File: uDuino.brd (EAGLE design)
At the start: 86.4 x 26.3 mm, 20 parts, among them IC1 LM7805, IC2 ATMEGA328, J1 POWER_JACK", Q1 16MHZ

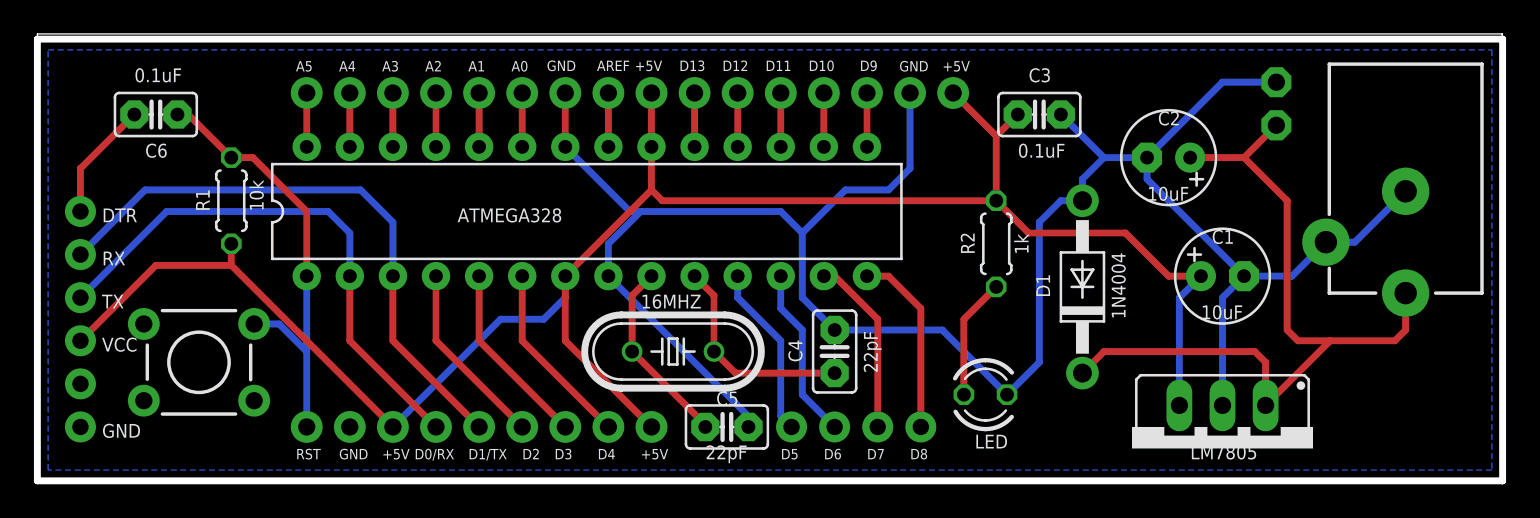
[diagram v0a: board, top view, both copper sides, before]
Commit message: Added LED at D13
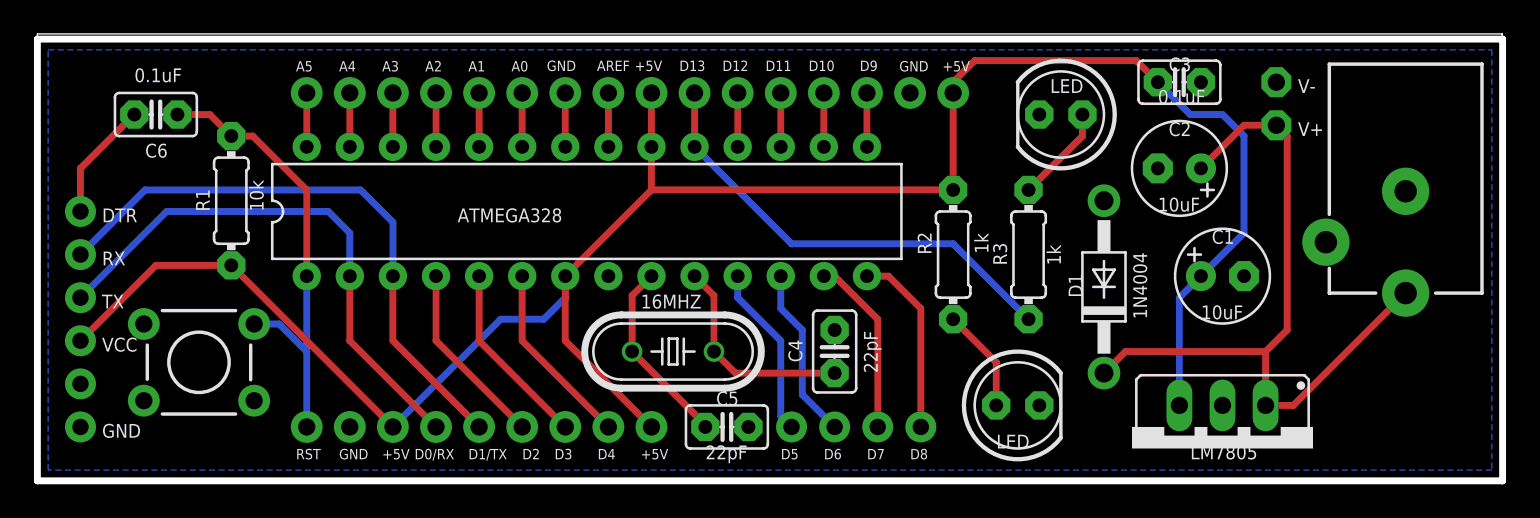
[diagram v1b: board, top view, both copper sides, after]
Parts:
- added LED2: GREEN, adafruit:LED5MM
- added R3: 1k, adafruit:0204/7
- LED1: device RBBB:LED -> adafruit:LED5MM
- R1, R2: device RBBB:RESISTOR -> adafruit:0204/7
- moved C3 8.47 mm to (67.3, 23.5)
- moved R2 2.62 mm to (54.0, 13.3)
- moved LED1 2.01 mm to (57.8, 4.45)
- moved D1 1.27 mm to (62.9, 11.4)
- moved C2 0.90 mm to (67.3, 18.4)
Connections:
- new net N$4: LED2.A, R3.1
- net D13: now also R3.2
- net GND: now also LED2.K
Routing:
- net GND: track 128.5 -> 3.81 mm
- net D13: track 3.18 -> 27.1 mm
- net +5V: track 115.8 -> 123.8 mm
- net N$4: track 0.00 -> 5.76 mm
- net N$1: track 46.3 -> 43.8 mm
- net N$5: track 7.14 -> 6.13 mm
- net RESET: track 26.5 -> 27.2 mm
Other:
- board text added: "R3"
- board text added: "V+"
- board text added: "V-"

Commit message: changed frame
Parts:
- added FRAME1: FRAME-LETTERNO_PACKAGE, SparkFun-Aesthetics:DUMMY
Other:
- board size 86.4 x 26.3 mm -> 86.4 x 26 mm
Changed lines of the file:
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@@
 <?xml version="1.0" encoding="utf-8"?>
 <!DOCTYPE eagle SYSTEM "eagle.dtd">
-<eagle version="8.0.1">
+<eagle version="8.2.1">
 <drawing>
 <settings>
@@
 <layer number="112" name="tSilk" color="7" fill="1" visible="yes" active="yes"/>
 <layer number="113" name="Paste_Add" color="7" fill="1" visible="yes" active="yes"/>
+<layer number="114" name="Badge_Outline" color="7" fill="1" visible="no" active="yes"/>
+<layer number="115" name="ReferenceISLANDS" color="7" fill="1" visible="no" active="yes"/>
 <layer number="116" name="Patch_BOT" color="7" fill="1" visible="yes" active="yes"/>
 <layer number="118" name="Rect_Pads" color="7" fill="1" visible="no" active="no"/>
@@
 <board>
 <plain>
-<wire x1="86.34" y1="0" x2="86.34" y2="26.34" width="0" layer="20"/>
-<wire x1="86.34" y1="26.34" x2="0" y2="26.34" width="0" layer="20"/>
-<wire x1="0" y1="26.34" x2="0" y2="26.035" width="0" layer="20"/>
-<wire x1="0" y1="0" x2="86.34" y2="0" width="0.4064" layer="20"/>
-<wire x1="86.34" y1="0" x2="86.36" y2="0" width="0.4064" layer="20"/>
-<wire x1="86.36" y1="0" x2="86.36" y2="26.035" width="0.4064" layer="20"/>
-<wire x1="86.36" y1="26.035" x2="0" y2="26.035" width="0.4064" layer="20"/>
-<wire x1="0" y1="26.035" x2="0" y2="0" width="0.4064" layer="20"/>
 <text x="31.75" y="24.765" size="0.6096" layer="21" font="vector" rot="R180">GND</text>
 <text x="34.925" y="24.765" size="0.6096" layer="21" font="vector" rot="R180">AREF</text>
@@
 <text x="60.325" y="12.7" size="0.8128" layer="21" font="vector" rot="R90">1k</text>
 <text x="59.69" y="22.86" size="0.8128" layer="21" font="vector">LED</text>
+<wire x1="0" y1="0" x2="86.36" y2="0" width="0.4064" layer="20"/>
+<wire x1="86.36" y1="0" x2="86.36" y2="26.035" width="0.4064" layer="20"/>
+<wire x1="86.36" y1="26.035" x2="0" y2="26.035" width="0.4064" layer="20"/>
+<wire x1="0" y1="26.035" x2="0" y2="0" width="0.4064" layer="20"/>
 </plain>
 <attributes>
@@
 <element name="Q1" library="adafruit" package="HC49/S" value="16MHZ" x="37.465" y="7.62" smashed="yes" rot="R180">
 <attribute name="MF" value="" x="37.465" y="7.62" size="1.778" layer="27" rot="R180" display="off"/>
+<attribute name="MPN" value="" x="37.465" y="7.62" size="1.778" layer="27" rot="R180" display="off"/>
+<attribute name="OC_FARNELL" value="1667008" x="37.465" y="7.62" size="1.778" layer="27" rot="R180" display="off"/>
 <attribute name="OC_NEWARK" value="unknown" x="37.465" y="7.62" size="1.778" layer="27" rot="R180" display="off"/>
-<attribute name="OC_FARNELL" value="1667008" x="37.465" y="7.62" size="1.778" layer="27" rot="R180" display="off"/>
-<attribute name="MPN" value="" x="37.465" y="7.62" size="1.778" layer="27" rot="R180" display="off"/>
 </element>
 <element name="C4" library="RBBB" package="UNPOLARIZED_CAP" value="22pF" x="46.99" y="7.62" smashed="yes" rot="R90"/>
@@
 <element name="R3" library="adafruit" package="0204/7" value="1k" x="58.42" y="13.335" smashed="yes" rot="R270"/>
 <element name="LED2" library="adafruit" package="LED5MM" value="GREEN" x="60.325" y="21.59" smashed="yes" rot="R180"/>
+<element name="FRAME1" library="SparkFun-Aesthetics" package="DUMMY" value="FRAME-LETTERNO_PACKAGE" x="0" y="0">
+<attribute name="DESIGNER" value="Ajay Meena" x="0" y="0" size="1.778" layer="27" display="off"/>
+<attribute name="VERSION" value="v01" x="0" y="0" size="1.778" layer="27" display="off"/>
+</element>
 </elements>
 <signals>
